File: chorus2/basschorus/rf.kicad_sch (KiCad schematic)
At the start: 12 parts, among them U11 TL072, U8 TL072

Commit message: code implementation
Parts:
- removed U11, U8: TL072, kicad-legacy/Housings_DIP.pretty:DIP-8_W7.62mm, symbol Amplifier_Operational:TL072
- added U4: TL074, symbol Amplifier_Operational:TL074
- renumbered R34 to R21, R35 to R22, R18 to R23, R18 to R24, R19 to R25
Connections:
- net OUT: now also U4.8, U4.9 (-)
- net at C22.2, R25.1: now also U4.10 (+)
- net at C19.2, R22.1: now also U4.5 (+)
- net at C20.1, R23.2: now also U4.6 (-), U4.7
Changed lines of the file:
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@@
 		(on_board yes)
 		(dnp no)
-		(property "Reference" "R19"
+		(property "Reference" "R25"
 			(at 180.34 97.6122 90)
 			(effects
@@
 			(project "basschorus"
 				(path "/7f3b4bac-3b2a-4af0-92ae-ccc3fcedc393/89406d17-d719-4016-b0cb-a2835ffb8d3f"
-					(reference "R19")
+					(reference "R25")
 					(unit 1)
 				)
@@
 		(on_board yes)
 		(dnp no)
-		(property "Reference" "R18"
+		(property "Reference" "R24"
 			(at 166.37 97.6122 90)
 			(effects
@@
 			(project "basschorus"
 				(path "/7f3b4bac-3b2a-4af0-92ae-ccc3fcedc393/89406d17-d719-4016-b0cb-a2835ffb8d3f"
-					(reference "R18")
-					(unit 1)
-				)
-			)
-		)
-	)
-	(symbol
-		(lib_id "Amplifier_Operational:TL072")
-		(at 128.27 102.87 0)
-		(unit 2)
-		(exclude_from_sim no)
-		(in_bom yes)
-		(on_board yes)
-		(dnp no)
-		(property "Reference" "U11"
-			(at 128.27 93.5482 0)
-			(effects
-				(font
-					(size 1.27 1.27)
-				)
-			)
-		)
-		(property "Value" "TL072"
-			(at 128.27 95.8596 0)
-			(effects
-				(font
-					(size 1.27 1.27)
-				)
-			)
-		)
-		(property "Footprint" "kicad-legacy/Housings_DIP.pretty:DIP-8_W7.62mm"
-			(at 128.27 102.87 0)
-			(effects
-				(font
-					(size 1.27 1.27)
-				)
-				(hide yes)
-			)
-		)
-		(property "Datasheet" "http://www.ti.com/lit/ds/symlink/tl071.pdf"
-			(at 128.27 102.87 0)
-			(effects
-				(font
-					(size 1.27 1.27)
-				)
-				(hide yes)
-			)
-		)
-		(property "Description" ""
-			(at 128.27 102.87 0)
-			(effects
-				(font
-					(size 1.27 1.27)
-				)
-			)
-		)
-		(pin "1"
-		)
-		(pin "2"
-		)
-		(pin "3"
-		)
-		(pin "5"
-		)
-		(pin "6"
-		)
-		(pin "7"
-		)
-		(pin "4"
-		)
-		(pin "8"
-		)
-		(instances
-			(project "basschorus"
-				(path "/7f3b4bac-3b2a-4af0-92ae-ccc3fcedc393/89406d17-d719-4016-b0cb-a2835ffb8d3f"
-					(reference "U11")
-					(unit 2)
+					(reference "R24")
+					(unit 1)
 				)
 			)
@@
 		(on_board yes)
 		(dnp no)
-		(property "Reference" "R35"
+		(property "Reference" "R22"
 			(at 106.68 95.0722 90)
 			(effects
@@
 			(project "basschorus"
 				(path "/7f3b4bac-3b2a-4af0-92ae-ccc3fcedc393/89406d17-d719-4016-b0cb-a2835ffb8d3f"
-					(reference "R35")
+					(reference "R22")
 					(unit 1)
 				)
@@
 		(on_board yes)
 		(dnp no)
-		(property "Reference" "R34"
+		(property "Reference" "R21"
 			(at 92.71 95.0722 90)
 			(effects
@@
 			(project "basschorus"
 				(path "/7f3b4bac-3b2a-4af0-92ae-ccc3fcedc393/89406d17-d719-4016-b0cb-a2835ffb8d3f"
-					(reference "R34")
+					(reference "R21")
 					(unit 1)
 				)
@@
 	)
 	(symbol
-		(lib_id "Amplifier_Operational:TL072")
+		(lib_id "Amplifier_Operational:TL074")
 		(at 201.93 105.41 0)
-		(unit 2)
-		(exclude_from_sim no)
-		(in_bom yes)
-		(on_board yes)
-		(dnp no)
-		(property "Reference" "U8"
-			(at 201.93 96.0882 0)
-			(effects
-				(font
-					(size 1.27 1.27)
-				)
-			)
-		)
-		(property "Value" "TL072"
-			(at 201.93 98.3996 0)
-			(effects
-				(font
-					(size 1.27 1.27)
-				)
-			)
-		)
-		(property "Footprint" "kicad-legacy/Housings_DIP.pretty:DIP-8_W7.62mm"
+		(unit 3)
+		(exclude_from_sim no)
+		(in_bom yes)
+		(on_board yes)
+		(dnp no)
+		(fields_autoplaced yes)
+		(property "Reference" "U4"
+			(at 201.93 95.885 0)
+			(effects
+				(font
+					(size 1.27 1.27)
+				)
+			)
+		)
+		(property "Value" "TL074"
+			(at 201.93 98.425 0)
+			(effects
+				(font
+					(size 1.27 1.27)
+				)
+			)
+		)
+		(property "Footprint" ""
+			(at 200.66 102.87 0)
+			(effects
+				(font
+					(size 1.27 1.27)
+				)
+				(hide yes)
+			)
+		)
+		(property "Datasheet" "http://www.ti.com/lit/ds/symlink/tl071.pdf"
+			(at 203.2 100.33 0)
+			(effects
+				(font
+					(size 1.27 1.27)
+				)
+				(hide yes)
+			)
+		)
+		(property "Description" "Quad Low-Noise JFET-Input Operational Amplifiers, DIP-14/SOIC-14"
 			(at 201.93 105.41 0)
 			(effects
@@
 			)
 		)
-		(property "Datasheet" "http://www.ti.com/lit/ds/symlink/tl071.pdf"
-			(at 201.93 105.41 0)
-			(effects
-				(font
-					(size 1.27 1.27)
-				)
-				(hide yes)
-			)
-		)
-		(property "Description" ""
-			(at 201.93 105.41 0)
-			(effects
-				(font
-					(size 1.27 1.27)
-				)
-			)
-		)
-		(pin "1"
-		)
-		(pin "2"
+		(pin "1"
 		)
 		(pin "3"
 		)
+		(pin "2"
+		)
 		(pin "5"
 		)
+		(pin "14"
+		)
+		(pin "10"
+		)
+		(pin "8"
+		)
 		(pin "6"
 		)
+		(pin "9"
+		)
+		(pin "11"
+		)
+		(pin "12"
+		)
 		(pin "7"
 		)
+		(pin "13"
+		)
 		(pin "4"
 		)
-		(pin "8"
-		)
-		(instances
-			(project "basschorus"
-				(path "/7f3b4bac-3b2a-4af0-92ae-ccc3fcedc393/89406d17-d719-4016-b0cb-a2835ffb8d3f"
-					(reference "U8")
-					(unit 2)
+		(instances
+			(project ""
+				(path "/7f3b4bac-3b2a-4af0-92ae-ccc3fcedc393/89406d17-d719-4016-b0cb-a2835ffb8d3f"
+					(reference "U4")
+					(unit 3)
 				)
 			)
@@
 		(on_board yes)
 		(dnp no)
-		(property "Reference" "R18"
+		(property "Reference" "R23"
 			(at 153.67 97.6122 90)
 			(effects
@@
 			(project "basschorus"
 				(path "/7f3b4bac-3b2a-4af0-92ae-ccc3fcedc393/89406d17-d719-4016-b0cb-a2835ffb8d3f"
-					(reference "R18")
+					(reference "R23")
 					(unit 1)
 				)
@@
 		(dnp no)
 		(fields_autoplaced yes)
-		(property "Reference" "#PWR043"
+		(property "Reference" "#PWR047"
 			(at 160.02 123.19 0)
 			(effects
@@
 			(project "basschorus"
 				(path "/7f3b4bac-3b2a-4af0-92ae-ccc3fcedc393/89406d17-d719-4016-b0cb-a2835ffb8d3f"
-					(reference "#PWR043")
+					(reference "#PWR047")
 					(unit 1)
 				)
@@
 		(dnp no)
 		(fields_autoplaced yes)
-		(property "Reference" "#PWR047"
+		(property "Reference" "#PWR048"
 			(at 187.96 123.19 0)
 			(effects
@@
 			(project "basschorus"
 				(path "/7f3b4bac-3b2a-4af0-92ae-ccc3fcedc393/89406d17-d719-4016-b0cb-a2835ffb8d3f"
-					(reference "#PWR047")
+					(reference "#PWR048")
 					(unit 1)
 				)
@@
 				)
 			)
+		)
+	)
+	(symbol
+		(lib_id "Amplifier_Operational:TL074")
+		(at 128.27 102.87 0)
+		(unit 2)
+		(exclude_from_sim no)
+		(in_bom yes)
+		(on_board yes)
+		(dnp no)
+		(property "Reference" "U4"
+			(at 128.27 92.71 0)
+			(effects
+				(font
+					(size 1.27 1.27)
+				)
+			)
+		)
+		(property "Value" "TL074"
+			(at 128.27 95.25 0)
+			(effects
+				(font
+					(size 1.27 1.27)
+				)
+			)
+		)
+		(property "Footprint" ""
+			(at 127 100.33 0)
+			(effects
+				(font
+					(size 1.27 1.27)
+				)
+				(hide yes)
+			)
+		)
+		(property "Datasheet" "http://www.ti.com/lit/ds/symlink/tl071.pdf"
+			(at 129.54 97.79 0)
+			(effects
+				(font
+					(size 1.27 1.27)
+				)
+				(hide yes)
+			)
+		)
+		(property "Description" "Quad Low-Noise JFET-Input Operational Amplifiers, DIP-14/SOIC-14"
+			(at 128.27 102.87 0)
+			(effects
+				(font
+					(size 1.27 1.27)
+				)
+				(hide yes)
+			)
+		)
+		(pin "1"
+		)
+		(pin "3"
+		)
+		(pin "2"
+		)
+		(pin "5"
+		)
+		(pin "14"
+		)
+		(pin "10"
+		)
+		(pin "8"
+		)
+		(pin "6"
+		)
+		(pin "9"
+		)
+		(pin "11"
+		)
+		(pin "12"
+		)
+		(pin "7"
+		)
+		(pin "13"
+		)
+		(pin "4"
+		)
+		(instances
+			(project ""
+				(path "/7f3b4bac-3b2a-4af0-92ae-ccc3fcedc393/89406d17-d719-4016-b0cb-a2835ffb8d3f"
+					(reference "U4")
+					(unit 2)
+				)
+			)

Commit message: update filters
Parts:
- added C28: 1u, symbol Device:C
- added R38: 10k, kicad-legacy/kicad-footprints/Resistor_THT.pretty:R_Axial_DIN0204_L3.6mm_D1.6mm_P2.54mm_Vertical, symbol Device:R
- C19: value 470p -> 4.7n
- C21: value 3.3n -> 4.7n
- C22: value 150p -> 470p
- C23: value 2.2n -> 4.7n
- R22: renamed from R21; value 91K -> 10k
- R23: renamed from R22; value 30K -> 22k
- R24: renamed from R23; value 11k -> 10k
- R25: renamed from R24; value 75K -> 56k
- R26: renamed from R25; value 51K -> 10k
- renumbered U4 to U2
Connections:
- net GND: now also U2.5 (+)
- net IN: now also C28.1; no longer R22.2
- net at R22.1, R23.2: now also C19.2, R38.2; no longer C20.2
- net at C20.1, R24.2, U2.7: now also R38.1; no longer U2.6 (-)
- new net: C20.2, R23.1, U2.6 (-)
- new net: C28.2, R22.2
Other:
- note added: "2nd order MF + 1st order passive + 2nd order SK -36db at 10kHz"
- note added: "dc blocking hp fc=16Hz"
- note removed: "5th order LPF (cascade 2nd sk + 1st passtive + 2nd sk) Butterworth, Cutoff = 4477Hz From textbook, Q1=.618 Q2=1.620 http://sim.okawa-denshi.jp/en/Sallen3tool.php http://sim.okawa-denshi.jp/en/OPstool.php"
- moved on the sheet: C19, C20

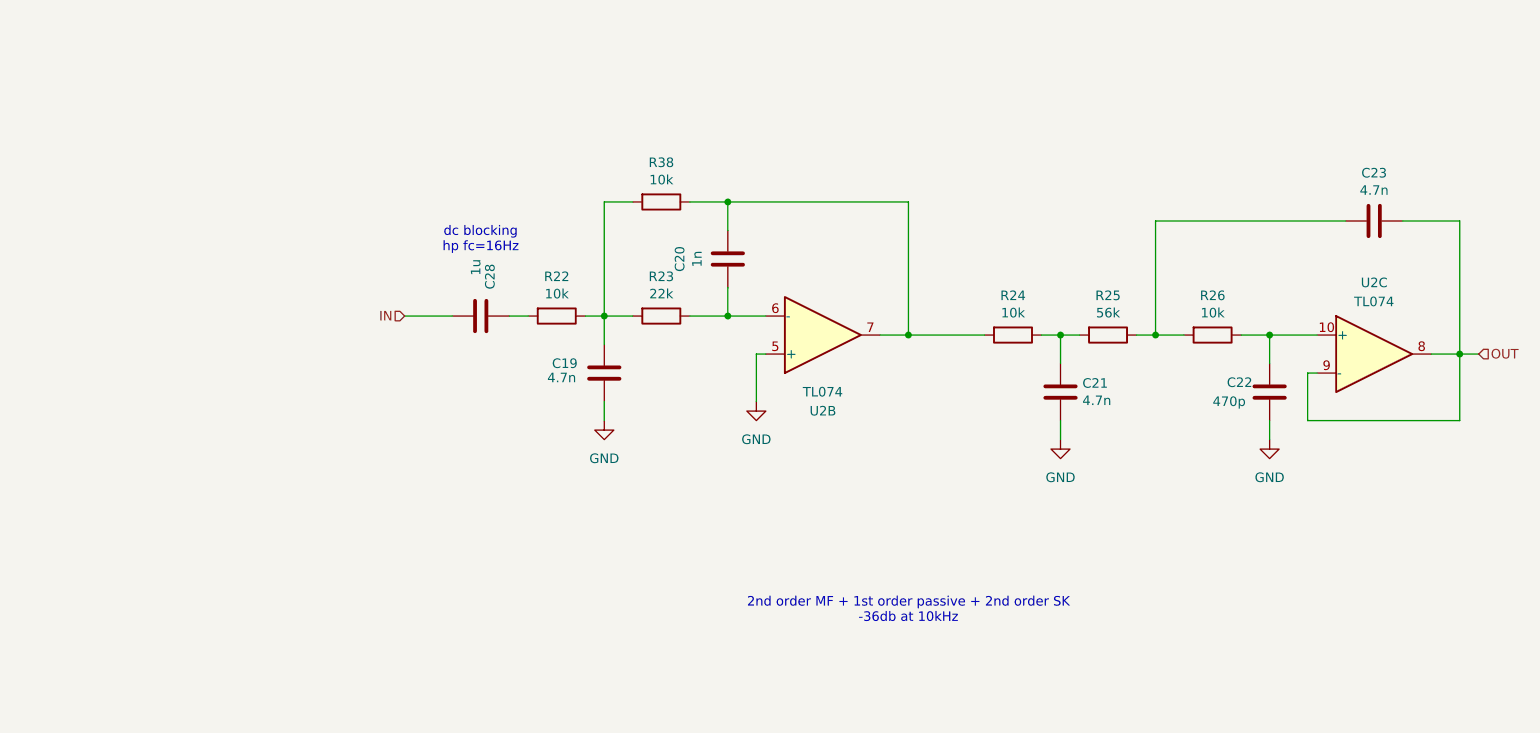
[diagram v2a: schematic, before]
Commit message: update designs based on new calculations
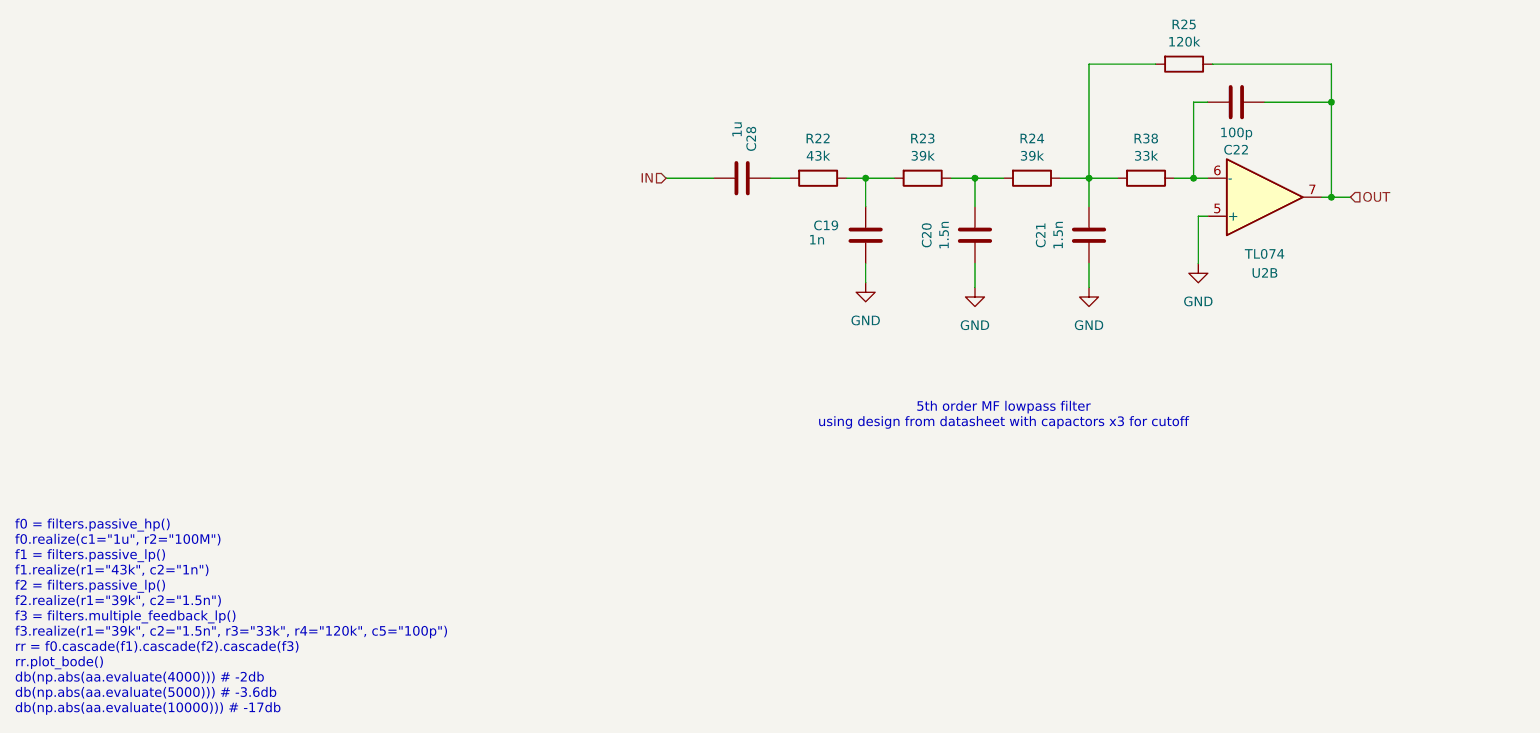
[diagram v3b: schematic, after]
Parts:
- removed C23: 4.7n, symbol Device:C
- removed R26: 10k, kicad-legacy/kicad-footprints/Resistor_THT.pretty:R_Axial_DIN0204_L3.6mm_D1.6mm_P2.54mm_Vertical, symbol Device:R
- removed unit 3 of U2
- C19: value 4.7n -> 1n
- C20: value 1n -> 1.5n
- C21: value 4.7n -> 1.5n
- C22: value 470p -> 100p
- R22: value 10k -> 43k
- R23: value 22k -> 39k
- R24: value 10k -> 39k
- R25: value 56k -> 120k
- R38: value 10k -> 33k
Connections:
- net GND: now also C20.2, C21.2; no longer C21.1, C22.1
- net OUT: now also C22.2, R25.1, U2.7
- net at R24.1, R25.2: now also C21.1, R38.2; no longer C21.2
- net at C19.2, R22.1, R23.2: no longer R38.2
- net at C20.1, R24.2: now also R23.1; no longer R38.1, U2.7
- new net: C22.1, R38.1, U2.6 (-)
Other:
- note added: "5th order MF lowpass filter using design from datasheet with capactors x3 for cutoff"
- note added: "f0 = filters.passive_hp() f0.realize(c1="1u", r2="100M") f1 = filters.passive_lp() f1.realize(r1="43k", c2="1n") f2 = filters.passive_lp() f2.realize(r1="39k", c2="1.5n") f3 = filters.multiple_feedback_lp() f3.realize(r1="39k", c2="1.5n", r3="33k", r4="120k", c5="100p") rr = f0.cascade(f1).cascade(f2).cascade(f3) rr.plot_bode() db(np.abs(aa.evaluate(4000))) # -2db db(np.abs(aa.evaluate(5000))) # 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"
- note removed: "2nd order MF + 1st order passive + 2nd order SK -36db at 10kHz"
- note removed: "dc blocking hp fc=16Hz"
- moved on the sheet: C19, C20, C28, R22, R23, R38
